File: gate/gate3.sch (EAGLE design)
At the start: 32 parts, among them J1 MOLEX_MINILITE_TRAP_2, J2 MOLEX_MINILITE_TRAP_2, J3 MOLEX_MINILITE_TRAP_2, J4 MOLEX_MINILITE_TRAP_2, J8 MOLEX_MINILITE_TRAP_2, J9 MOLEX_MINILITE_TRAP_2, U1 SN75468

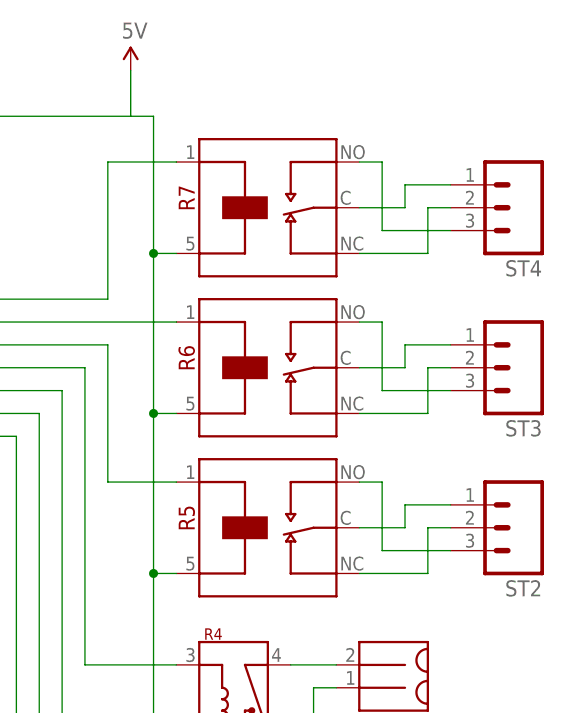
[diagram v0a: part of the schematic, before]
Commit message: Fix gate3 relay and ps orientation
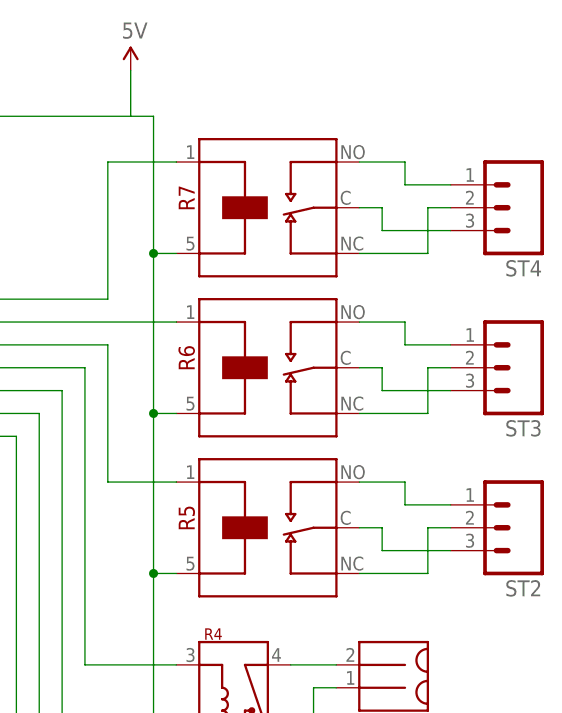
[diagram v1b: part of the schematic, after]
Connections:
- removed net N$22: R5.NO, ST2.3
- new net N$25: R7.NO, ST4.1
- net N$14: now also R6.NO; no longer R6.C
- net N$16: now also R5.NO; no longer R5.C
- net N$17: now also R5.C, ST2.3; no longer R6.NO, ST3.3
- net N$18: now also R6.C, ST3.3; no longer R7.C, ST4.1
- net N$20: now also R7.C; no longer R7.NO
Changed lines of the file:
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@@
-</segment>
-</net>
-<net name="N$16" class="0">
-<segment>
-<pinref part="R5" gate="G$1" pin="C"/>
-<wire x1="154.94" y1="73.66" x2="160.02" y2="73.66" width="0.1524" layer="91"/>
-<wire x1="160.02" y1="73.66" x2="160.02" y2="76.2" width="0.1524" layer="91"/>
-<pinref part="ST2" gate="G$1" pin="1"/>
-<wire x1="160.02" y1="76.2" x2="165.1" y2="76.2" width="0.1524" layer="91"/>
 </segment>
 </net>
@@
 </segment>
 </net>
-<net name="N$22" class="0">
-<segment>
-<pinref part="ST2" gate="G$1" pin="3"/>
-<wire x1="165.1" y1="71.12" x2="157.48" y2="71.12" width="0.1524" layer="91"/>
-<wire x1="157.48" y1="71.12" x2="157.48" y2="78.74" width="0.1524" layer="91"/>
-<pinref part="R5" gate="G$1" pin="NO"/>
-<wire x1="157.48" y1="78.74" x2="154.94" y2="78.74" width="0.1524" layer="91"/>
-</segment>
-</net>
-<net name="N$14" class="0">
-<segment>
-<pinref part="R6" gate="G$1" pin="C"/>
-<wire x1="154.94" y1="91.44" x2="160.02" y2="91.44" width="0.1524" layer="91"/>
-<wire x1="160.02" y1="91.44" x2="160.02" y2="93.98" width="0.1524" layer="91"/>
-<pinref part="ST3" gate="G$1" pin="1"/>
-<wire x1="160.02" y1="93.98" x2="165.1" y2="93.98" width="0.1524" layer="91"/>
-</segment>
-</net>
 <net name="N$15" class="0">
 <segment>
@@
 <pinref part="R6" gate="G$1" pin="NC"/>
 <wire x1="162.56" y1="86.36" x2="154.94" y2="86.36" width="0.1524" layer="91"/>
-</segment>
-</net>
-<net name="N$17" class="0">
-<segment>
-<pinref part="ST3" gate="G$1" pin="3"/>
-<wire x1="165.1" y1="88.9" x2="157.48" y2="88.9" width="0.1524" layer="91"/>
-<wire x1="157.48" y1="88.9" x2="157.48" y2="96.52" width="0.1524" layer="91"/>
-<pinref part="R6" gate="G$1" pin="NO"/>
-<wire x1="157.48" y1="96.52" x2="154.94" y2="96.52" width="0.1524" layer="91"/>
-</segment>
-</net>
-<net name="N$18" class="0">
-<segment>
-<pinref part="R7" gate="G$1" pin="C"/>
-<wire x1="154.94" y1="109.22" x2="160.02" y2="109.22" width="0.1524" layer="91"/>
-<wire x1="160.02" y1="109.22" x2="160.02" y2="111.76" width="0.1524" layer="91"/>
-<pinref part="ST4" gate="G$1" pin="1"/>
-<wire x1="160.02" y1="111.76" x2="165.1" y2="111.76" width="0.1524" layer="91"/>
 </segment>
 </net>
@@
 <net name="N$20" class="0">
 <segment>
-<pinref part="R7" gate="G$1" pin="NO"/>
-<wire x1="154.94" y1="114.3" x2="157.48" y2="114.3" width="0.1524" layer="91"/>
-<wire x1="157.48" y1="114.3" x2="157.48" y2="106.68" width="0.1524" layer="91"/>
 <pinref part="ST4" gate="G$1" pin="3"/>
 <wire x1="157.48" y1="106.68" x2="165.1" y2="106.68" width="0.1524" layer="91"/>
+<pinref part="R7" gate="G$1" pin="C"/>
+<wire x1="157.48" y1="106.68" x2="157.48" y2="109.22" width="0.1524" layer="91"/>
+<wire x1="157.48" y1="109.22" x2="154.94" y2="109.22" width="0.1524" layer="91"/>
 </segment>
 </net>
+<net name="N$25" class="0">
+<segment>
+<pinref part="R7" gate="G$1" pin="NO"/>
+<pinref part="ST4" gate="G$1" pin="1"/>
+<wire x1="160.02" y1="111.76" x2="165.1" y2="111.76" width="0.1524" layer="91"/>
+<wire x1="154.94" y1="114.3" x2="160.02" y2="114.3" width="0.1524" layer="91"/>
+<wire x1="160.02" y1="114.3" x2="160.02" y2="111.76" width="0.1524" layer="91"/>
+</segment>
+</net>
+<net name="N$14" class="0">
+<segment>
+<pinref part="R6" gate="G$1" pin="NO"/>
+<wire x1="154.94" y1="96.52" x2="160.02" y2="96.52" width="0.1524" layer="91"/>
+<wire x1="160.02" y1="96.52" x2="160.02" y2="93.98" width="0.1524" layer="91"/>
+<pinref part="ST3" gate="G$1" pin="1"/>
+<wire x1="160.02" y1="93.98" x2="165.1" y2="93.98" width="0.1524" layer="91"/>
+</segment>
+</net>
+<net name="N$16" class="0">
+<segment>
+<pinref part="R5" gate="G$1" pin="NO"/>
+<wire x1="154.94" y1="78.74" x2="160.02" y2="78.74" width="0.1524" layer="91"/>
+<wire x1="160.02" y1="78.74" x2="160.02" y2="76.2" width="0.1524" layer="91"/>
+<pinref part="ST2" gate="G$1" pin="1"/>
+<wire x1="160.02" y1="76.2" x2="165.1" y2="76.2" width="0.1524" layer="91"/>
+</segment>
+</net>
+<net name="N$17" class="0">
+<segment>
+<pinref part="R5" gate="G$1" pin="C"/>
+<wire x1="154.94" y1="73.66" x2="157.48" y2="73.66" width="0.1524" layer="91"/>
+<wire x1="157.48" y1="73.66" x2="157.48" y2="71.12" width="0.1524" layer="91"/>
+<pinref part="ST2" gate="G$1" pin="3"/>
+<wire x1="157.48" y1="71.12" x2="165.1" y2="71.12" width="0.1524" layer="91"/>
+</segment>
+</net>
+<net name="N$18" class="0">
+<segment>
+<pinref part="R6" gate="G$1" pin="C"/>
+<wire x1="154.94" y1="91.44" x2="157.48" y2="91.44" width="0.1524" layer="91"/>
+<wire x1="157.48" y1="91.44" x2="157.48" y2="88.9" width="0.1524" layer="91"/>
+<pinref part="ST3" gate="G$1" pin="3"/>
+<wire x1="157.48" y1="88.9" x2="165.1" y2="88.9" width="0.1524" layer="91"/>
+</segment>
+</net>
